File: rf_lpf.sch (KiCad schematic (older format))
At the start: 0 parts

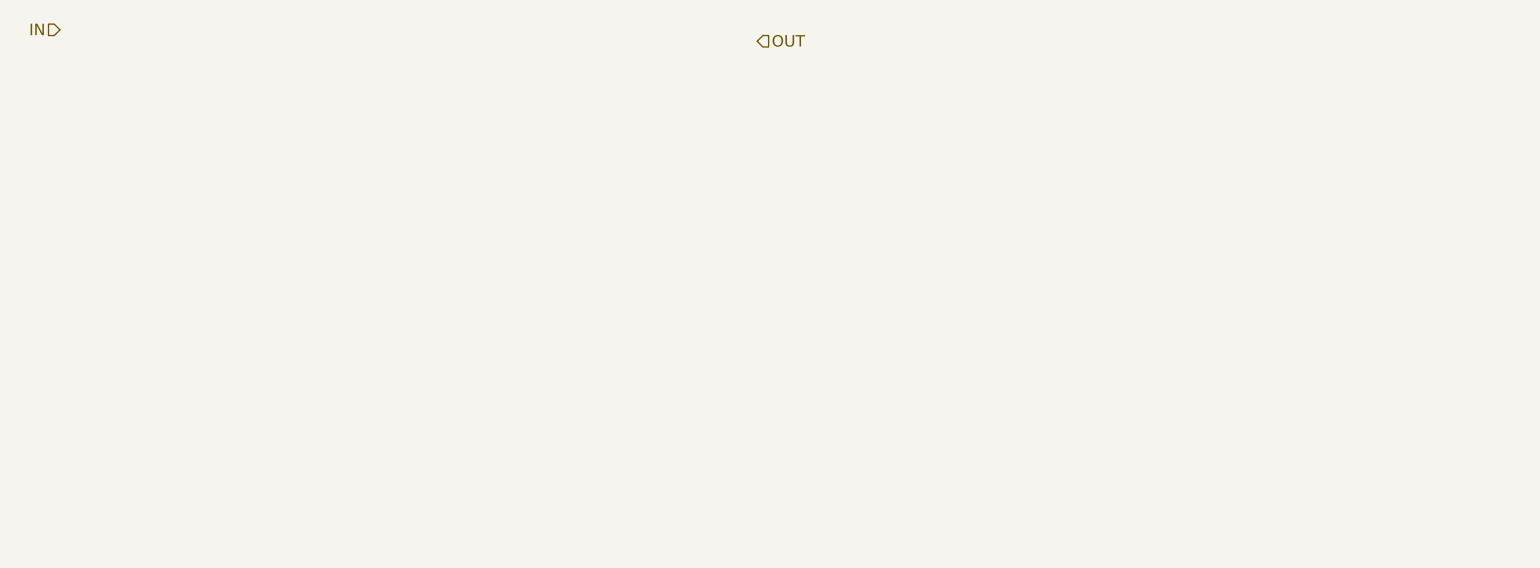
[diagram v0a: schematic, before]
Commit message: RF filter implemented
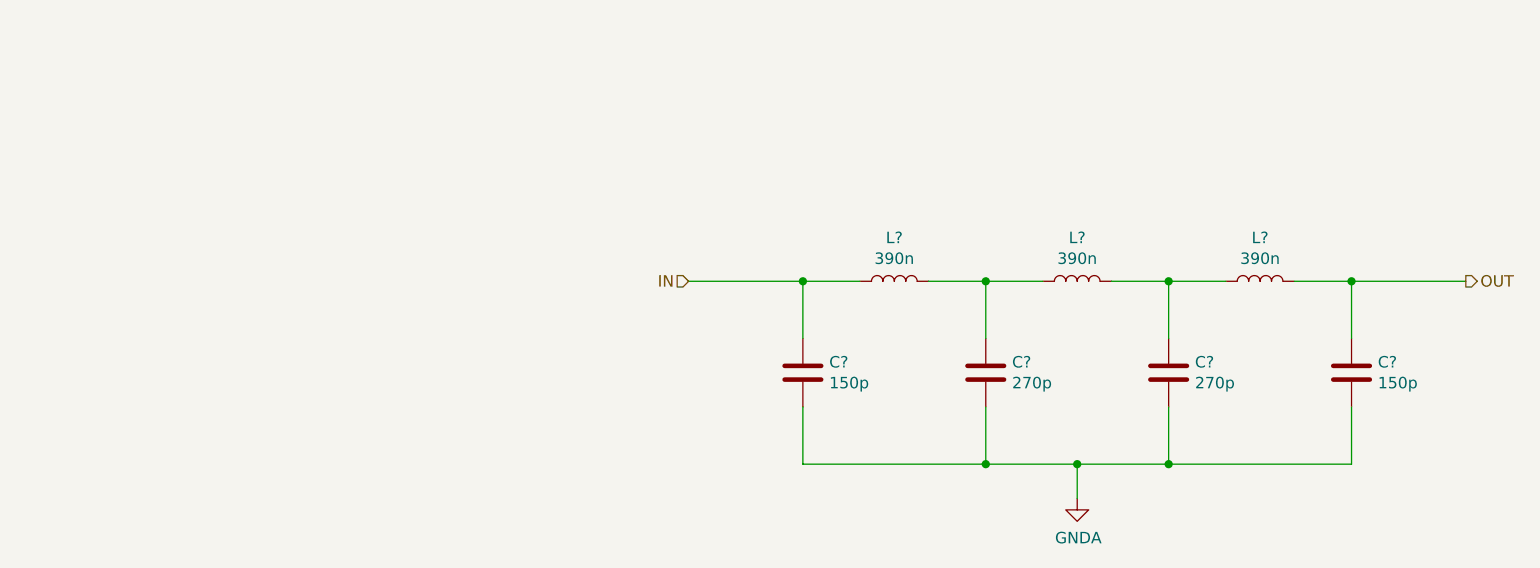
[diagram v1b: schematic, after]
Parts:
- added C? (x2): 150p, symbol Device:C
- added C? (x2): 270p, symbol Device:C
- added L? (x3): 390n, symbol Device:L
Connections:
- net IN: now also C?.1, L?.1
- net OUT: now also C?.1, L?.2
- new net: C?.1, L?.1, L?.2 (x2)
- new net GNDA: C?.2, C?.2, C?.2, C?.2
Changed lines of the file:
@@
 encoding utf-8
 Sheet 2 8
-Title ""
-Date ""
-Rev ""
-Comp ""
-Comment1 ""
-Comment2 ""
-Comment3 ""
-Comment4 ""
+Title "HF-SDR RF-LPF"
+Date "2020 december"
+Rev "v01"
+Comp "by Keri"
+Comment1 "-42,17 dB @ 44 MHz"
+Comment2 "-3 dB @ 29,56 MHz"
+Comment3 "50 Ohm input/output impedance"
+Comment4 "30 MHz low pass filter"
 $EndDescr
-Text HLabel 1450 2300 0    50   Input ~ 0
+Text HLabel 4200 3400 0    50   Input ~ 0
 IN
-Text HLabel 4500 2350 2    50   Input ~ 0
+Text HLabel 7600 3400 2    50   Output ~ 0
 OUT
+$Comp
+L Device:L L?
+U 1 1 5FE3619B
+P 5100 3400
+F 0 "L?" V 5290 3400 50  0000 C CNN
+F 1 "390n" V 5199 3400 50  0000 C CNN
+F 2 "" H 5100 3400 50  0001 C CNN
+F 3 "~" H 5100 3400 50  0001 C CNN
+	1    5100 3400
+	0    -1   -1   0
+$EndComp
+$Comp
+L Device:L L?
+U 1 1 5FE3661E
+P 5900 3400
+F 0 "L?" V 6090 3400 50  0000 C CNN
+F 1 "390n" V 5999 3400 50  0000 C CNN
+F 2 "" H 5900 3400 50  0001 C CNN
+F 3 "~" H 5900 3400 50  0001 C CNN
+	1    5900 3400
+	0    -1   -1   0
+$EndComp
+$Comp
+L Device:L L?
+U 1 1 5FE3686B
+P 6700 3400
+F 0 "L?" V 6890 3400 50  0000 C CNN
+F 1 "390n" V 6799 3400 50  0000 C CNN
+F 2 "" H 6700 3400 50  0001 C CNN
+F 3 "~" H 6700 3400 50  0001 C CNN
+	1    6700 3400
+	0    -1   -1   0
+$EndComp
+$Comp
+L Device:C C?
+U 1 1 5FE36C7C
+P 4700 3800
+F 0 "C?" H 4815 3846 50  0000 L CNN
+F 1 "150p" H 4815 3755 50  0000 L CNN
+F 2 "" H 4738 3650 50  0001 C CNN
+F 3 "~" H 4700 3800 50  0001 C CNN
+	1    4700 3800
+	1    0    0    -1
+$EndComp
+$Comp
+L Device:C C?
+U 1 1 5FE36EEB
+P 7100 3800
+F 0 "C?" H 7215 3846 50  0000 L CNN
+F 1 "150p" H 7215 3755 50  0000 L CNN
+F 2 "" H 7138 3650 50  0001 C CNN
+F 3 "~" H 7100 3800 50  0001 C CNN
+	1    7100 3800
+	1    0    0    -1
+$EndComp
+$Comp
+L Device:C C?
+U 1 1 5FE370C8
+P 5500 3800
+F 0 "C?" H 5615 3846 50  0000 L CNN
+F 1 "270p" H 5615 3755 50  0000 L CNN
+F 2 "" H 5538 3650 50  0001 C CNN
+F 3 "~" H 5500 3800 50  0001 C CNN
+	1    5500 3800
+	1    0    0    -1
+$EndComp
+$Comp
+L Device:C C?
+U 1 1 5FE373A2
+P 6300 3800
+F 0 "C?" H 6415 3846 50  0000 L CNN
+F 1 "270p" H 6415 3755 50  0000 L CNN
+F 2 "" H 6338 3650 50  0001 C CNN
+F 3 "~" H 6300 3800 50  0001 C CNN
+	1    6300 3800
+	1    0    0    -1
+$EndComp
+Wire Wire Line
+	4700 3650 4700 3400
+Wire Wire Line
+	4700 3400 4950 3400
+Wire Wire Line
+	5250 3400 5500 3400
+Wire Wire Line
+	6050 3400 6300 3400
+Wire Wire Line
+	6850 3400 7100 3400
+Wire Wire Line
+	7100 3650 7100 3400
+Connection ~ 7100 3400
+Wire Wire Line
+	7100 3400 7600 3400
+Wire Wire Line
+	6300 3650 6300 3400
+Connection ~ 6300 3400
+Wire Wire Line
+	6300 3400 6550 3400
+Wire Wire Line
+	5500 3650 5500 3400
+Connection ~ 5500 3400
+Wire Wire Line
+	5500 3400 5750 3400
+Wire Wire Line
+	4700 3950 4700 4200
+Wire Wire Line
+	4700 4200 5500 4200
+Wire Wire Line
+	7100 4200 7100 3950
+Wire Wire Line
+	6300 3950 6300 4200
+Connection ~ 6300 4200
+Wire Wire Line
+	6300 4200 7100 4200
+Wire Wire Line
+	5500 3950 5500 4200
+Connection ~ 5500 4200
+Wire Wire Line
+	5500 4200 5900 4200
+Wire Wire Line
+	4700 3400 4200 3400
+Connection ~ 4700 3400
+Wire Wire Line
+	5900 4200 5900 4350
+Connection ~ 5900 4200
+Wire Wire Line
+	5900 4200 6300 4200
+$Comp
+L power:GNDA #PWR?
+U 1 1 5FE4B301
+P 5900 4350
+F 0 "#PWR?" H 5900 4100 50  0001 C CNN
+F 1 "GNDA" H 5905 4177 50  0000 C CNN
+F 2 "" H 5900 4350 50  0001 C CNN
+F 3 "" H 5900 4350 50  0001 C CNN
+	1    5900 4350
+	1    0    0    -1
+$EndComp
 $EndSCHEMATC

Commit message: Initalize receiver test circuit
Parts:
- C1, C2, C3, C4: renamed from C?; footprint (none) -> Capacitor_SMD:C_0805_2012Metric_Pad1.18x1.45mm_HandSolder
- L1: renamed from L?; footprint (none) -> Inductor_SMD:L_1206_3216Metric_Pad1.22x1.90mm_HandSolder; Lomex (none) -> 93-00-46
- L2, L3: renamed from L?; footprint (none) -> Inductor_SMD:L_1206_3216Metric_Pad1.22x1.90mm_HandSolder
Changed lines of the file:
@@
 $Descr A4 11693 8268
 encoding utf-8
-Sheet 2 9
+Sheet 2 7
 Title "HF-SDR RF-LPF"
 Date "2020 december"
@@
 OUT
 $Comp
-L Device:L L?
+L Device:L L1
 U 1 1 5FE3619B
 P 5100 3400
-F 0 "L?" V 5290 3400 50  0000 C CNN
+F 0 "L1" V 5290 3400 50  0000 C CNN
 F 1 "390n" V 5199 3400 50  0000 C CNN
-F 2 "" H 5100 3400 50  0001 C CNN
+F 2 "Inductor_SMD:L_1206_3216Metric_Pad1.22x1.90mm_HandSolder" H 5100 3400 50  0001 C CNN
 F 3 "~" H 5100 3400 50  0001 C CNN
+F 4 "93-00-46" V 5050 3400 50  0000 C CNN "Lomex"
 	1    5100 3400
 	0    -1   -1   0
 $EndComp
 $Comp
-L Device:L L?
+L Device:L L2
 U 1 1 5FE3661E
 P 5900 3400
-F 0 "L?" V 6090 3400 50  0000 C CNN
+F 0 "L2" V 6090 3400 50  0000 C CNN
 F 1 "390n" V 5999 3400 50  0000 C CNN
-F 2 "" H 5900 3400 50  0001 C CNN
+F 2 "Inductor_SMD:L_1206_3216Metric_Pad1.22x1.90mm_HandSolder" H 5900 3400 50  0001 C CNN
 F 3 "~" H 5900 3400 50  0001 C CNN
 	1    5900 3400
@@
 $EndComp
 $Comp
-L Device:L L?
+L Device:L L3
 U 1 1 5FE3686B
 P 6700 3400
-F 0 "L?" V 6890 3400 50  0000 C CNN
+F 0 "L3" V 6890 3400 50  0000 C CNN
 F 1 "390n" V 6799 3400 50  0000 C CNN
-F 2 "" H 6700 3400 50  0001 C CNN
+F 2 "Inductor_SMD:L_1206_3216Metric_Pad1.22x1.90mm_HandSolder" H 6700 3400 50  0001 C CNN
 F 3 "~" H 6700 3400 50  0001 C CNN
 	1    6700 3400
@@
 $EndComp
 $Comp
-L Device:C C?
+L Device:C C1
 U 1 1 5FE36C7C
 P 4700 3800
-F 0 "C?" H 4815 3846 50  0000 L CNN
+F 0 "C1" H 4815 3846 50  0000 L CNN
 F 1 "150p" H 4815 3755 50  0000 L CNN
-F 2 "" H 4738 3650 50  0001 C CNN
+F 2 "Capacitor_SMD:C_0805_2012Metric_Pad1.18x1.45mm_HandSolder" H 4738 3650 50  0001 C CNN
 F 3 "~" H 4700 3800 50  0001 C CNN
 	1    4700 3800
@@
 $EndComp
 $Comp
-L Device:C C?
+L Device:C C4
 U 1 1 5FE36EEB
 P 7100 3800
-F 0 "C?" H 7215 3846 50  0000 L CNN
+F 0 "C4" H 7215 3846 50  0000 L CNN
 F 1 "150p" H 7215 3755 50  0000 L CNN
-F 2 "" H 7138 3650 50  0001 C CNN
+F 2 "Capacitor_SMD:C_0805_2012Metric_Pad1.18x1.45mm_HandSolder" H 7138 3650 50  0001 C CNN
 F 3 "~" H 7100 3800 50  0001 C CNN
 	1    7100 3800
@@
 $EndComp
 $Comp
-L Device:C C?
+L Device:C C2
 U 1 1 5FE370C8
 P 5500 3800
-F 0 "C?" H 5615 3846 50  0000 L CNN
+F 0 "C2" H 5615 3846 50  0000 L CNN
 F 1 "270p" H 5615 3755 50  0000 L CNN
-F 2 "" H 5538 3650 50  0001 C CNN
+F 2 "Capacitor_SMD:C_0805_2012Metric_Pad1.18x1.45mm_HandSolder" H 5538 3650 50  0001 C CNN
 F 3 "~" H 5500 3800 50  0001 C CNN
 	1    5500 3800
@@
 $EndComp
 $Comp
-L Device:C C?
+L Device:C C3
 U 1 1 5FE373A2
 P 6300 3800
-F 0 "C?" H 6415 3846 50  0000 L CNN
+F 0 "C3" H 6415 3846 50  0000 L CNN
 F 1 "270p" H 6415 3755 50  0000 L CNN
-F 2 "" H 6338 3650 50  0001 C CNN
+F 2 "Capacitor_SMD:C_0805_2012Metric_Pad1.18x1.45mm_HandSolder" H 6338 3650 50  0001 C CNN
 F 3 "~" H 6300 3800 50  0001 C CNN
 	1    6300 3800
@@
 	5900 4200 6300 4200
 $Comp
-L power:GNDA #PWR?
+L power:GNDA #PWR01
 U 1 1 5FE4B301
 P 5900 4350
-F 0 "#PWR?" H 5900 4100 50  0001 C CNN
+F 0 "#PWR01" H 5900 4100 50  0001 C CNN
 F 1 "GNDA" H 5905 4177 50  0000 C CNN
 F 2 "" H 5900 4350 50  0001 C CNN

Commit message: Nyáktervezésre majdnem kész
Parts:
- L1, L2, L3: footprint Inductor_SMD:L_1206_3216Metric_Pad1.22x1.90mm_HandSolder -> Inductor_SMD:L_1206_3216Metric_Pad1.42x1.75mm_HandSolder; Hestore (none) -> 100.321.35
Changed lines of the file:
@@
 F 0 "L1" V 5290 3400 50  0000 C CNN
 F 1 "390n" V 5199 3400 50  0000 C CNN
-F 2 "Inductor_SMD:L_1206_3216Metric_Pad1.22x1.90mm_HandSolder" H 5100 3400 50  0001 C CNN
+F 2 "Inductor_SMD:L_1206_3216Metric_Pad1.42x1.75mm_HandSolder" H 5100 3400 50  0001 C CNN
 F 3 "~" H 5100 3400 50  0001 C CNN
 F 4 "93-00-46" V 5050 3400 50  0000 C CNN "Lomex"
+F 5 "100.321.35" H 5100 3400 50  0001 C CNN "Hestore"
 	1    5100 3400
 	0    -1   -1   0
@@
 F 0 "L2" V 6090 3400 50  0000 C CNN
 F 1 "390n" V 5999 3400 50  0000 C CNN
-F 2 "Inductor_SMD:L_1206_3216Metric_Pad1.22x1.90mm_HandSolder" H 5900 3400 50  0001 C CNN
+F 2 "Inductor_SMD:L_1206_3216Metric_Pad1.42x1.75mm_HandSolder" H 5900 3400 50  0001 C CNN
 F 3 "~" H 5900 3400 50  0001 C CNN
+F 4 "100.321.35" H 5900 3400 50  0001 C CNN "Hestore"
 	1    5900 3400
 	0    -1   -1   0
@@
 F 0 "L3" V 6890 3400 50  0000 C CNN
 F 1 "390n" V 6799 3400 50  0000 C CNN
-F 2 "Inductor_SMD:L_1206_3216Metric_Pad1.22x1.90mm_HandSolder" H 6700 3400 50  0001 C CNN
+F 2 "Inductor_SMD:L_1206_3216Metric_Pad1.42x1.75mm_HandSolder" H 6700 3400 50  0001 C CNN
 F 3 "~" H 6700 3400 50  0001 C CNN
+F 4 "100.321.35" H 6700 3400 50  0001 C CNN "Hestore"
 	1    6700 3400
 	0    -1   -1   0

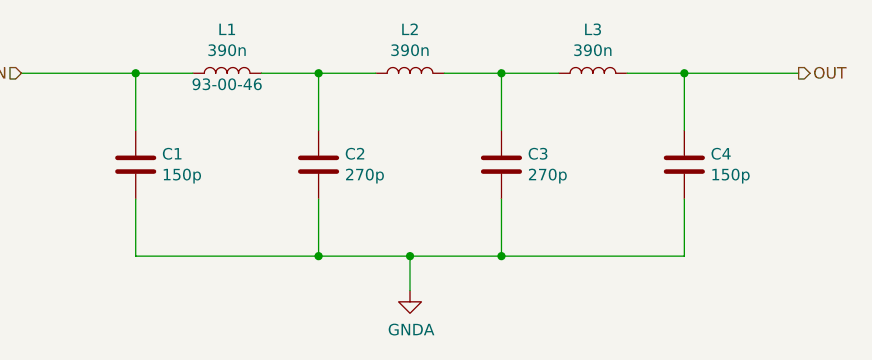
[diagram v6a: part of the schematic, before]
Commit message: FPGA change and new project file
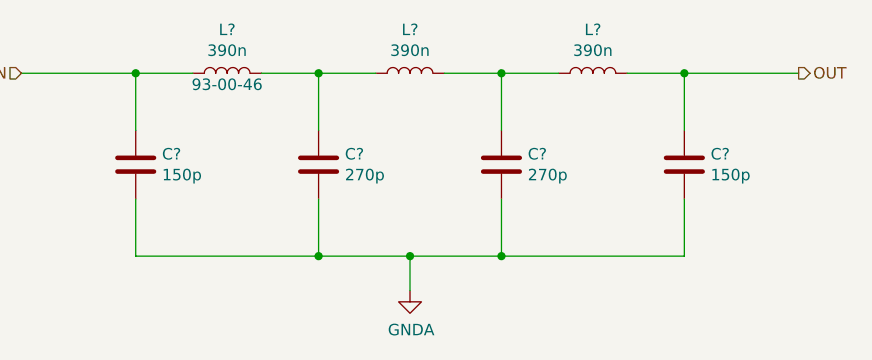
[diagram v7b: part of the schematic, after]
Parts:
- renumbered C1 to C?, C4 to C?, C2 to C?, C3 to C?, L1 to L?, L2 to L?, L3 to L?
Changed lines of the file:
@@
 $Descr A4 11693 8268
 encoding utf-8
-Sheet 2 7
+Sheet 2 12
 Title "30 MHz Lowpass filter"
 Date "2020 december"
@@
 OUT
 $Comp
-L Device:L L1
+L Device:L L?
 U 1 1 5FE3619B
 P 5100 3400
-F 0 "L1" V 5290 3400 50  0000 C CNN
+F 0 "L?" V 5290 3400 50  0000 C CNN
 F 1 "390n" V 5199 3400 50  0000 C CNN
 F 2 "Inductor_SMD:L_1206_3216Metric_Pad1.42x1.75mm_HandSolder" H 5100 3400 50  0001 C CNN
@@
 $EndComp
 $Comp
-L Device:L L2
+L Device:L L?
 U 1 1 5FE3661E
 P 5900 3400
-F 0 "L2" V 6090 3400 50  0000 C CNN
+F 0 "L?" V 6090 3400 50  0000 C CNN
 F 1 "390n" V 5999 3400 50  0000 C CNN
 F 2 "Inductor_SMD:L_1206_3216Metric_Pad1.42x1.75mm_HandSolder" H 5900 3400 50  0001 C CNN
@@
 $EndComp
 $Comp
-L Device:L L3
+L Device:L L?
 U 1 1 5FE3686B
 P 6700 3400
-F 0 "L3" V 6890 3400 50  0000 C CNN
+F 0 "L?" V 6890 3400 50  0000 C CNN
 F 1 "390n" V 6799 3400 50  0000 C CNN
 F 2 "Inductor_SMD:L_1206_3216Metric_Pad1.42x1.75mm_HandSolder" H 6700 3400 50  0001 C CNN
@@
 $EndComp
 $Comp
-L Device:C C1
+L Device:C C?
 U 1 1 5FE36C7C
 P 4700 3800
-F 0 "C1" H 4815 3846 50  0000 L CNN
+F 0 "C?" H 4815 3846 50  0000 L CNN
 F 1 "150p" H 4815 3755 50  0000 L CNN
 F 2 "Capacitor_SMD:C_0805_2012Metric_Pad1.18x1.45mm_HandSolder" H 4738 3650 50  0001 C CNN
@@
 $EndComp
 $Comp
-L Device:C C4
+L Device:C C?
 U 1 1 5FE36EEB
 P 7100 3800
-F 0 "C4" H 7215 3846 50  0000 L CNN
+F 0 "C?" H 7215 3846 50  0000 L CNN
 F 1 "150p" H 7215 3755 50  0000 L CNN
 F 2 "Capacitor_SMD:C_0805_2012Metric_Pad1.18x1.45mm_HandSolder" H 7138 3650 50  0001 C CNN
@@
 $EndComp
 $Comp
-L Device:C C2
+L Device:C C?
 U 1 1 5FE370C8
 P 5500 3800
-F 0 "C2" H 5615 3846 50  0000 L CNN
+F 0 "C?" H 5615 3846 50  0000 L CNN
 F 1 "270p" H 5615 3755 50  0000 L CNN
 F 2 "Capacitor_SMD:C_0805_2012Metric_Pad1.18x1.45mm_HandSolder" H 5538 3650 50  0001 C CNN
@@
 $EndComp
 $Comp
-L Device:C C3
+L Device:C C?
 U 1 1 5FE373A2
 P 6300 3800
-F 0 "C3" H 6415 3846 50  0000 L CNN
+F 0 "C?" H 6415 3846 50  0000 L CNN
 F 1 "270p" H 6415 3755 50  0000 L CNN
 F 2 "Capacitor_SMD:C_0805_2012Metric_Pad1.18x1.45mm_HandSolder" H 6338 3650 50  0001 C CNN
@@
 	5900 4200 6300 4200
 $Comp
-L power:GNDA #PWR01
+L power:GNDA #PWR?
 U 1 1 5FE4B301
 P 5900 4350
-F 0 "#PWR01" H 5900 4100 50  0001 C CNN
+F 0 "#PWR?" H 5900 4100 50  0001 C CNN
 F 1 "GNDA" H 5905 4177 50  0000 C CNN
 F 2 "" H 5900 4350 50  0001 C CNN
